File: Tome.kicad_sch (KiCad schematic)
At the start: 119 parts, among them J1 USB_C_Receptacle_USB2.0_14P, J2 [battery connector], J3 SD_Card_Receptacle, J4 [bootstrap jumper], J5 AudioJack3, J6 Conn_01x24_Socket, J7 Conn_01x24_Socket, Q1 DMG3415, Q2 DMG3415, Q3 Si1308EDL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

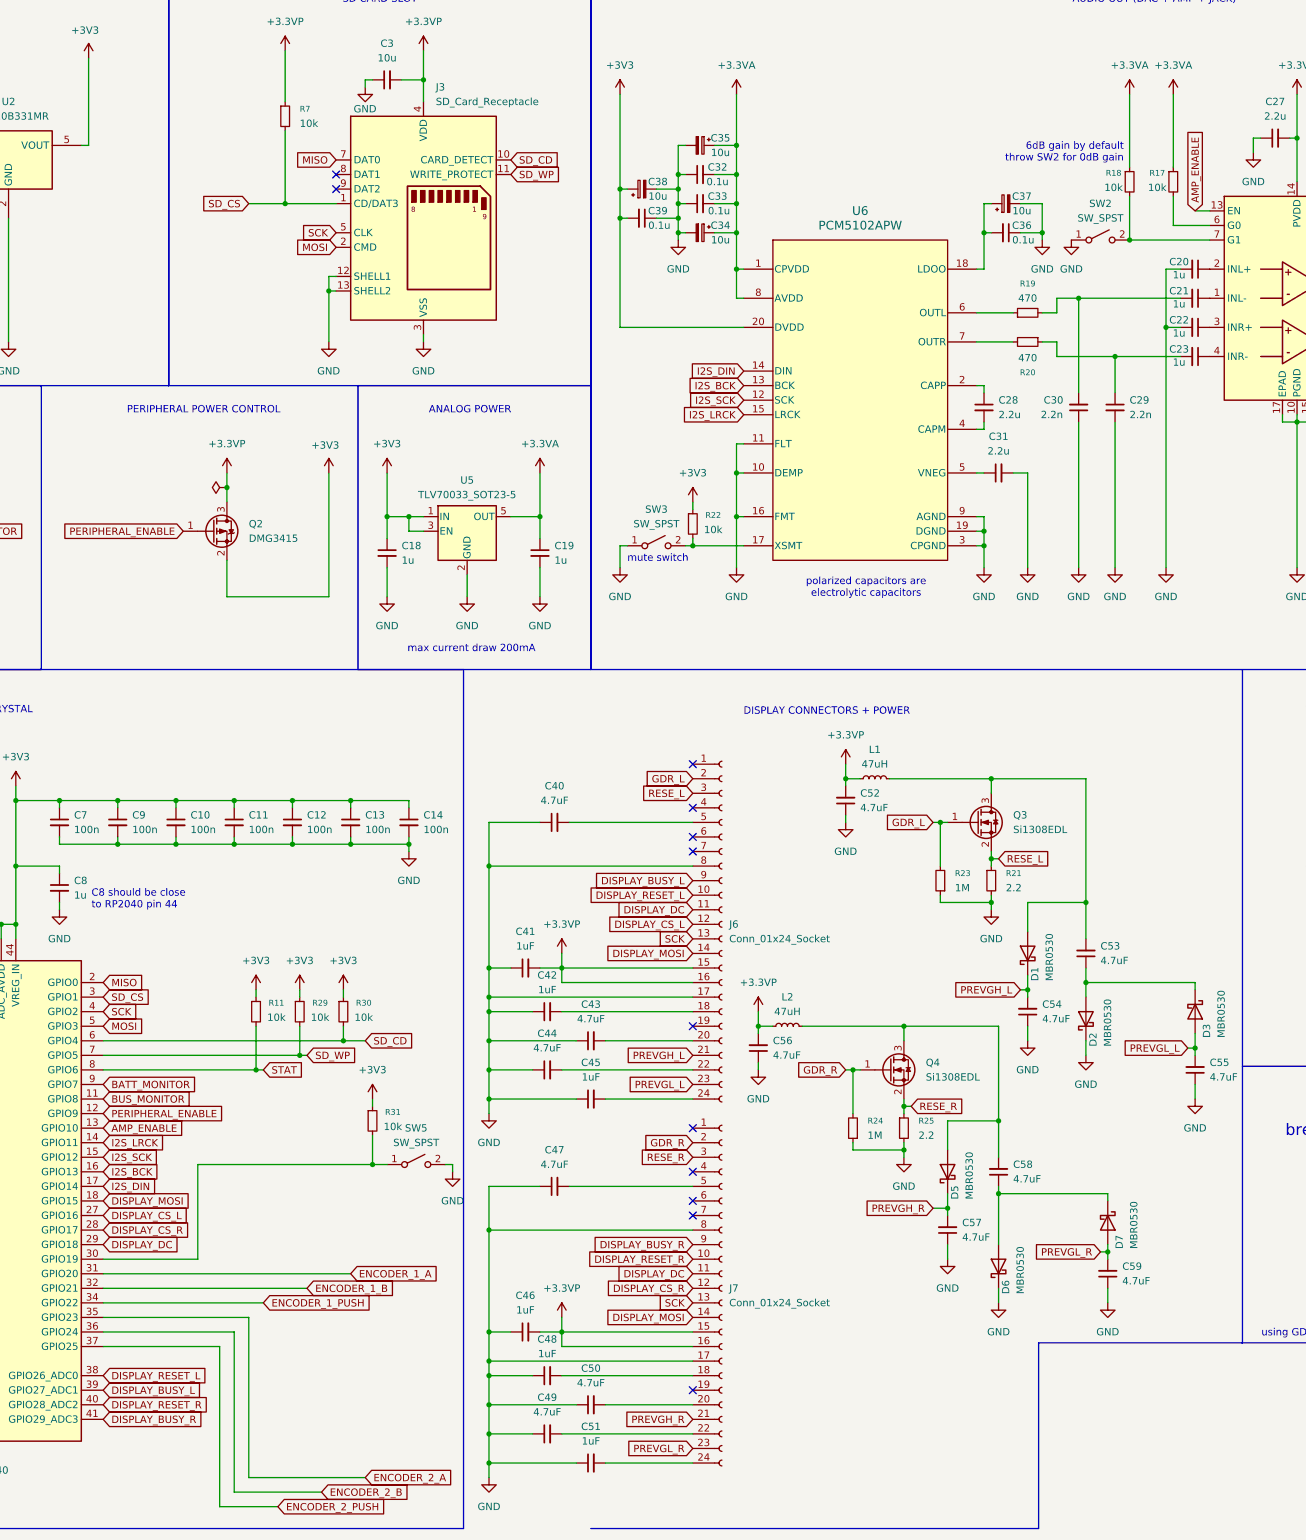
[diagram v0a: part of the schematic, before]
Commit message: adjusting pin assignments
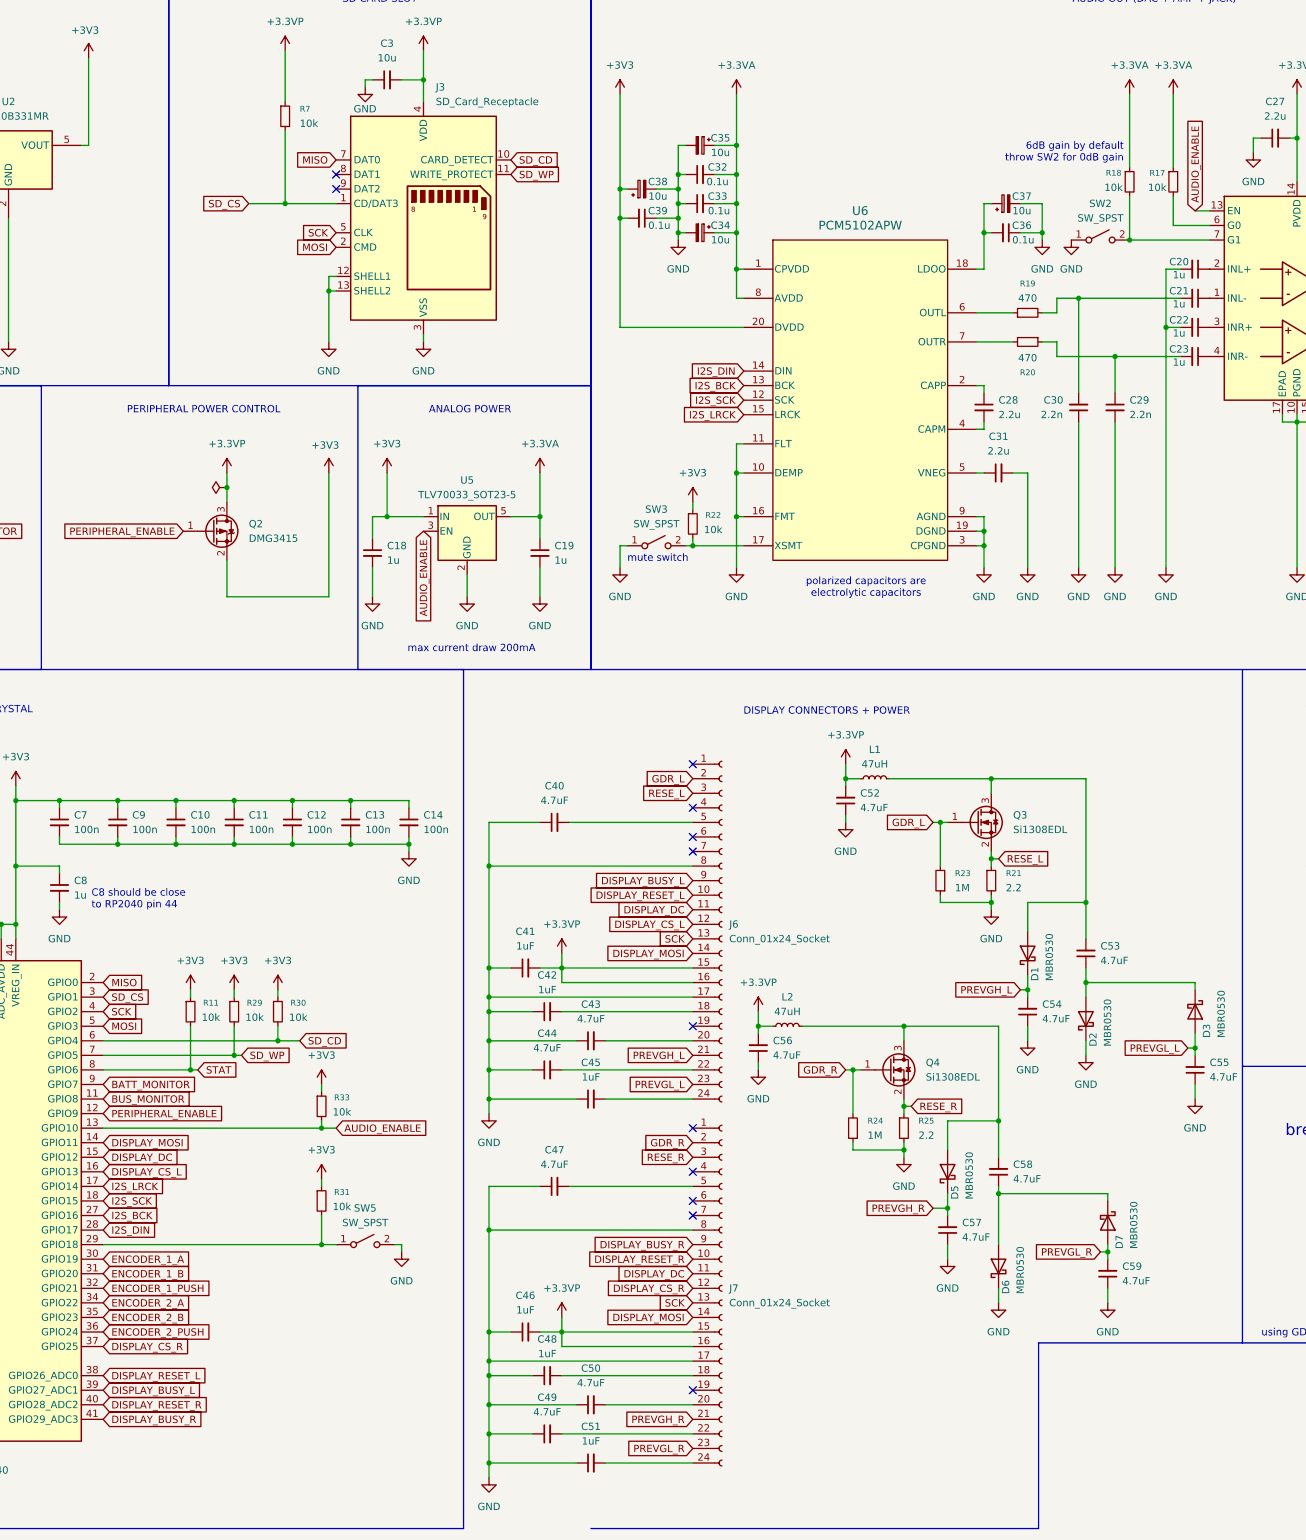
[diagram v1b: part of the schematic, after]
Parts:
- added R33: 10k, symbol Device:R_Small
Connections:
- net +3V3: now also R33.1; no longer U5.3 (EN)
- net DISPLAY_CS_L: now also U1.16 (GPIO13); no longer U1.27 (GPIO16)
- net DISPLAY_CS_R: now also U1.37 (GPIO25); no longer U1.28 (GPIO17)
- net DISPLAY_DC: now also U1.15 (GPIO12); no longer U1.29 (GPIO18)
- net DISPLAY_MOSI: now also U1.14 (GPIO11); no longer U1.18 (GPIO15)
- net ENCODER_1_A: now also U1.30 (GPIO19); no longer U1.31 (GPIO20)
- net ENCODER_1_B: now also U1.31 (GPIO20); no longer U1.32 (GPIO21)
- net ENCODER_1_PUSH: now also U1.32 (GPIO21); no longer U1.34 (GPIO22)
- net ENCODER_2_A: now also U1.34 (GPIO22); no longer U1.35 (GPIO23)
- net ENCODER_2_B: now also U1.35 (GPIO23); no longer U1.36 (GPIO24)
- net ENCODER_2_PUSH: now also U1.36 (GPIO24); no longer U1.37 (GPIO25)
- net I2S_BCK: now also U1.27 (GPIO16); no longer U1.16 (GPIO13)
- net I2S_DIN: now also U1.28 (GPIO17); no longer U1.17 (GPIO14)
- net I2S_LRCK: now also U1.17 (GPIO14); no longer U1.14 (GPIO11)
- net I2S_SCK: now also U1.18 (GPIO15); no longer U1.15 (GPIO12)
- net at R31.2, SW5.1 (A): now also U1.29 (GPIO18); no longer U1.30 (GPIO19)
- net AMP_ENABLE renamed AUDIO_ENABLE
- net AUDIO_ENABLE: now also U5.3 (EN), R33.2
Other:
- moved on the sheet: C18, R11, R29, R30, R31, SW5

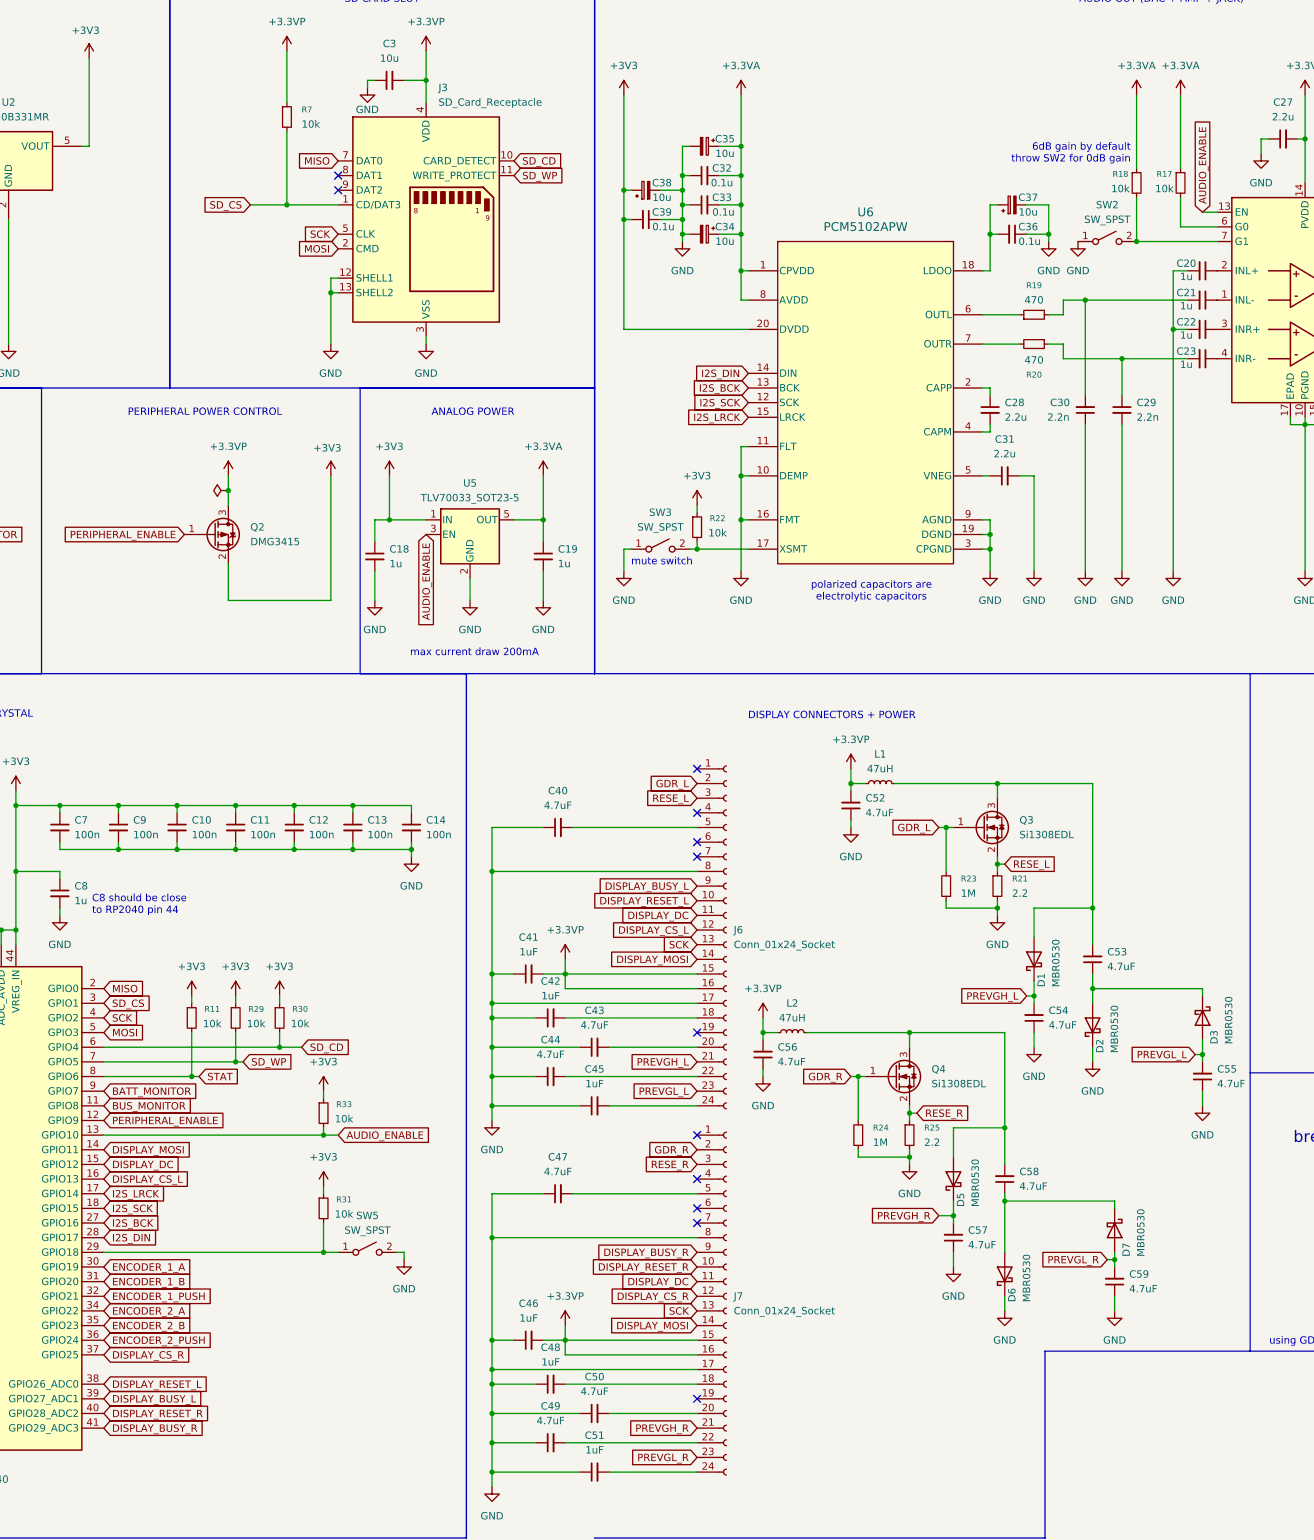
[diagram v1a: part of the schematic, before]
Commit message: fixing pullup resistors
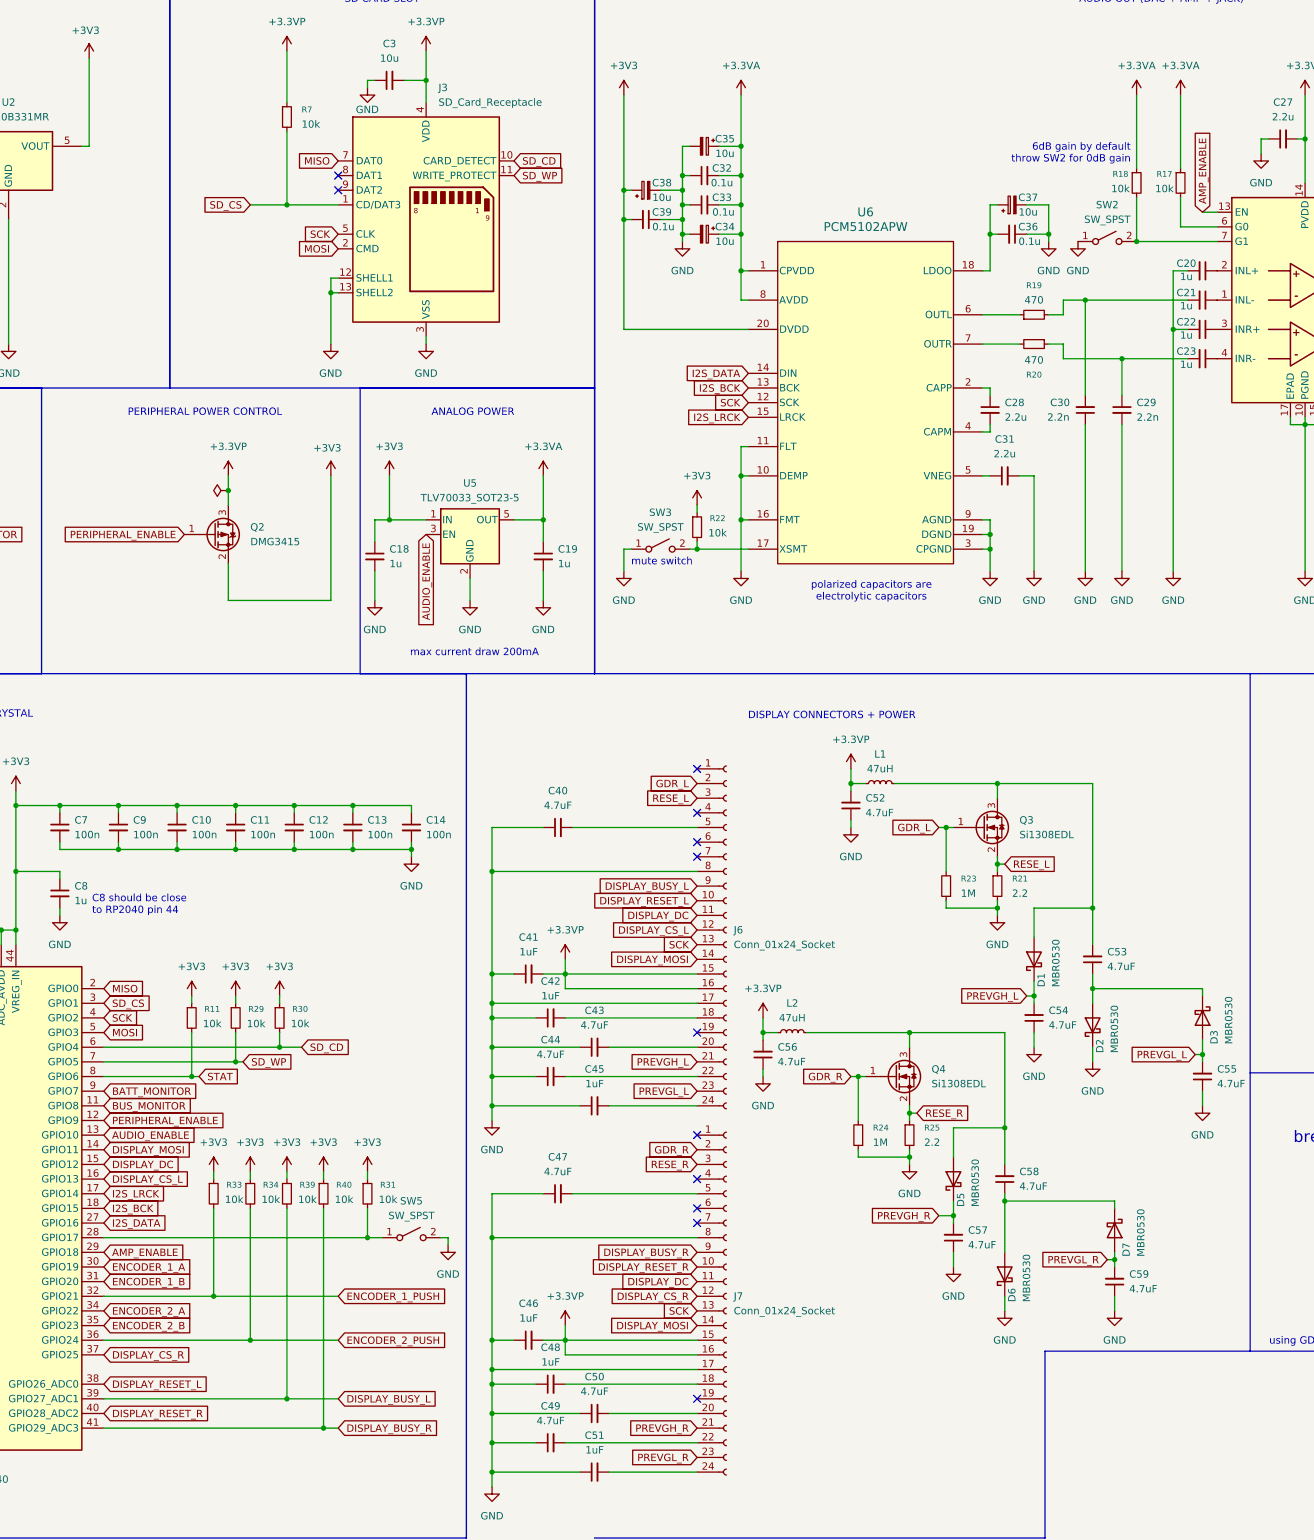
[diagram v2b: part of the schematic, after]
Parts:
- added R34, R39, R40: 10k, symbol Device:R_Small
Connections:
- net +3V3: now also R34.1, R39.1, R40.1
- net AUDIO_ENABLE: no longer R33.2, U7.13 (EN)
- net DISPLAY_BUSY_L: now also R39.2
- net DISPLAY_BUSY_R: now also R40.2
- net ENCODER_1_PUSH: now also R33.2
- net ENCODER_2_PUSH: now also R34.2
- net I2S_BCK: now also U1.18 (GPIO15); no longer U1.27 (GPIO16)
- net SCK: now also U6.12 (SCK)
- net at R31.2, SW5.1 (A): now also U1.28 (GPIO17); no longer U1.29 (GPIO18)
- net I2S_DIN renamed I2S_DATA
- net I2S_DATA: now also U1.27 (GPIO16); no longer U1.28 (GPIO17)
- removed net I2S_SCK: U1.18 (GPIO15), U6.12 (SCK)
- new net AMP_ENABLE: U1.29 (GPIO18), U7.13 (EN)
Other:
- moved on the sheet: R31, SW5

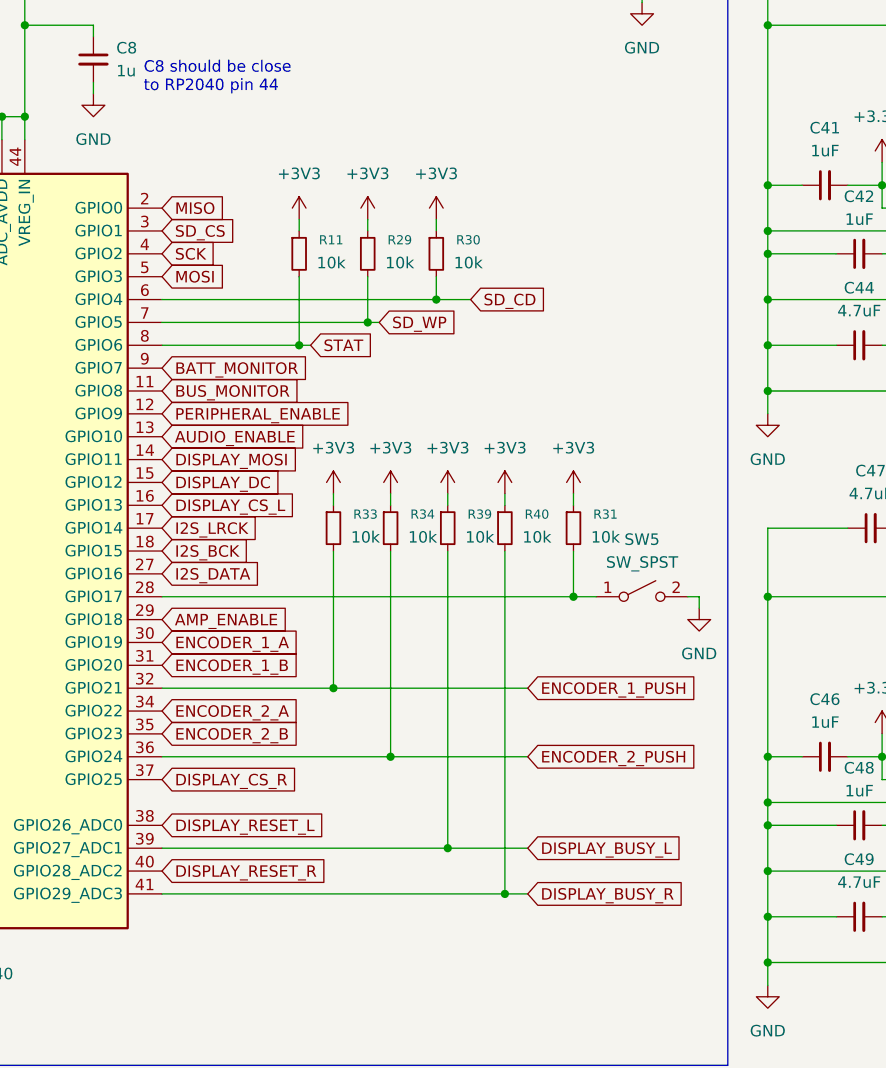
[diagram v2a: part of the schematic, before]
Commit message: removing incorrect pullups
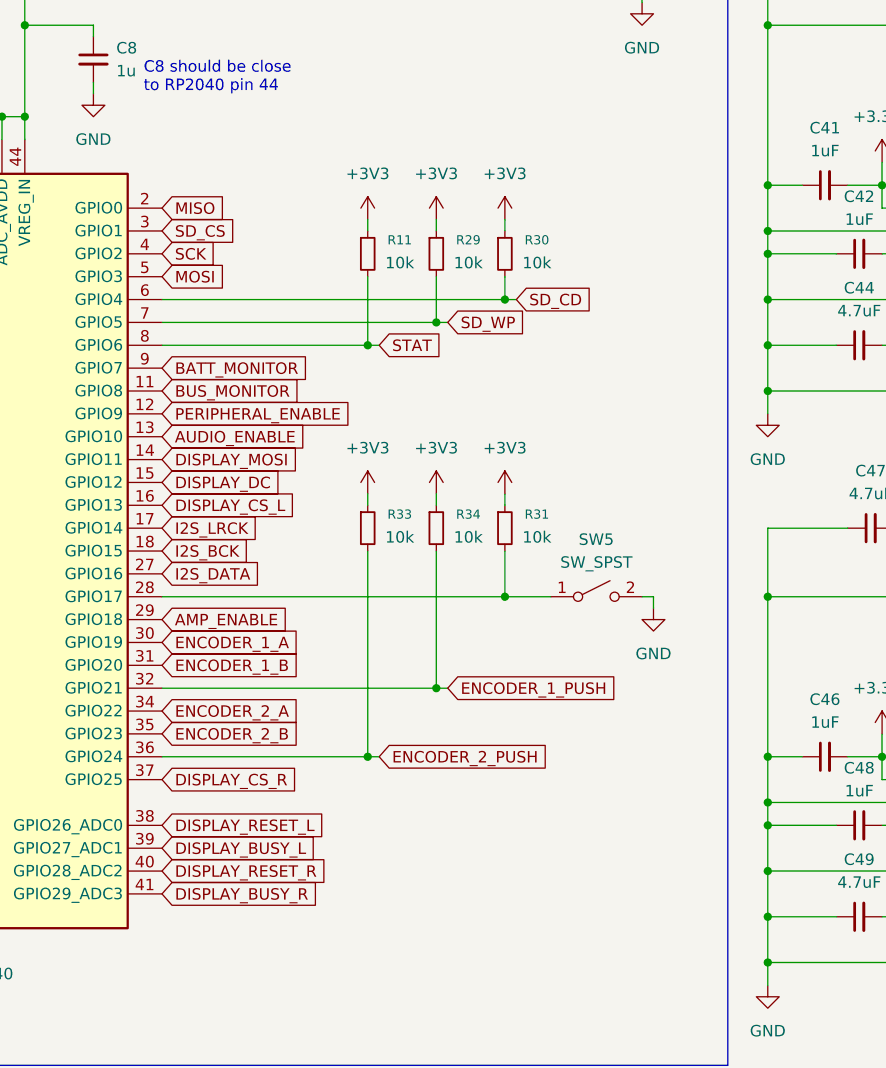
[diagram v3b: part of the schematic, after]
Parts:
- removed R39, R40: 10k, symbol Device:R_Small
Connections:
- net ENCODER_1_PUSH: now also R34.2; no longer R33.2
- net ENCODER_2_PUSH: now also R33.2; no longer R34.2
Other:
- moved on the sheet: R11, R29, R30, R31, R33, R34, SW5
